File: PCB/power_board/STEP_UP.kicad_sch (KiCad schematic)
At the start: 9 parts, among them IC11 TPS61032PWP, IC8 TPS63000IDRCRQ1

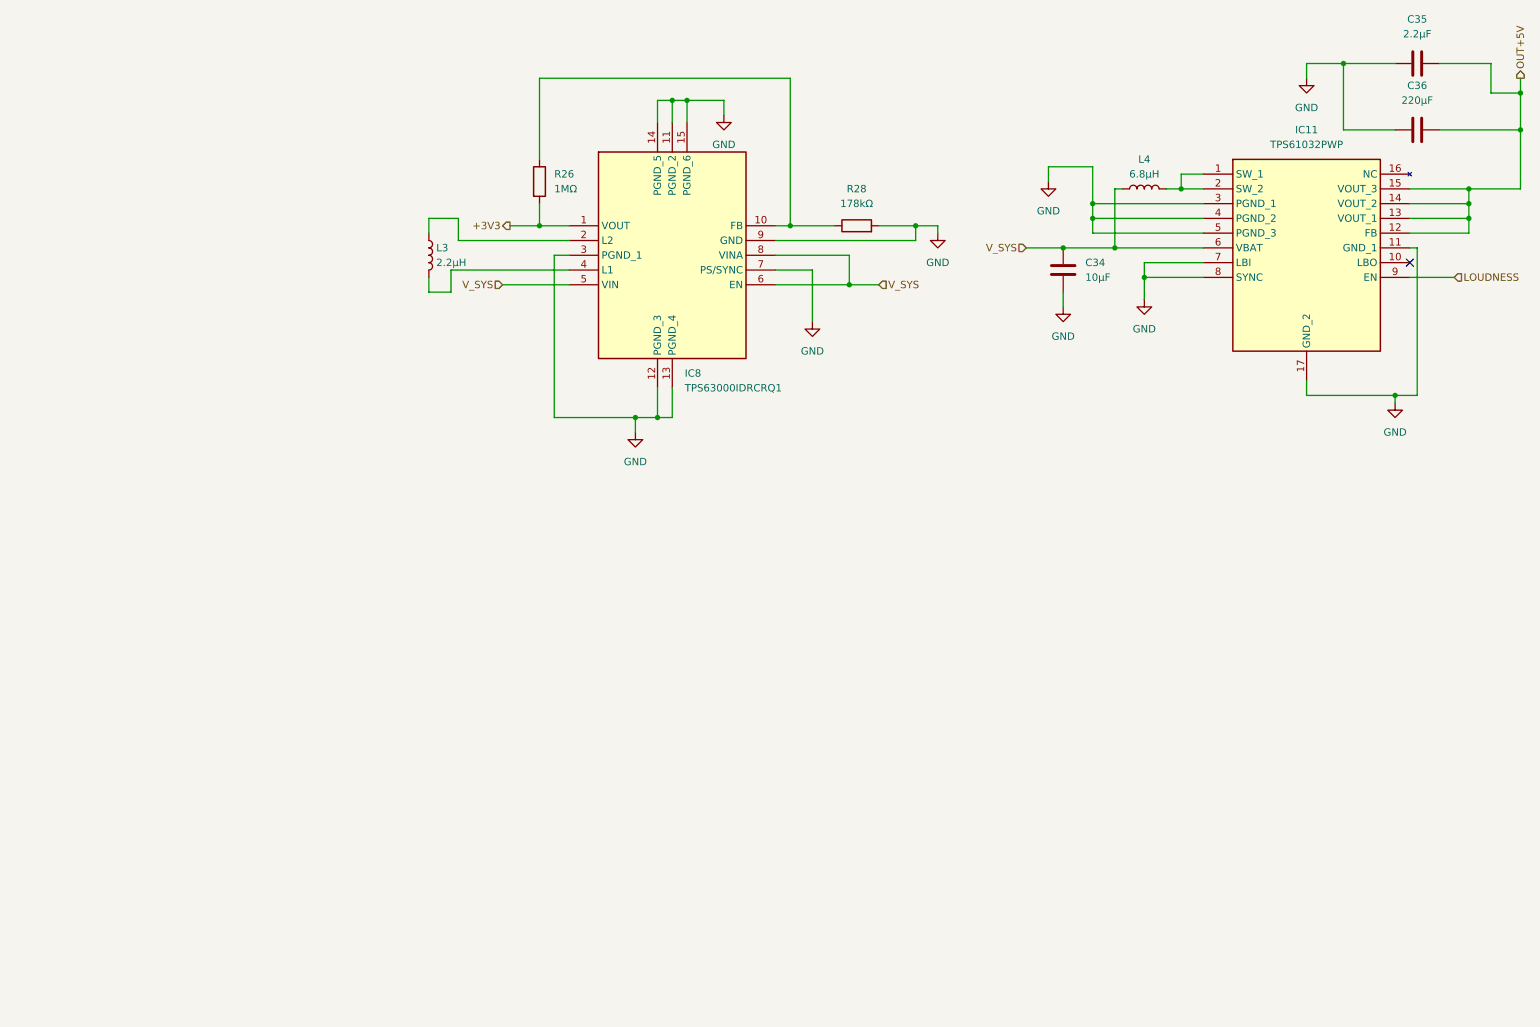
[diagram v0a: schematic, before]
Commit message: verifying schematic and 3V8 power for gsm
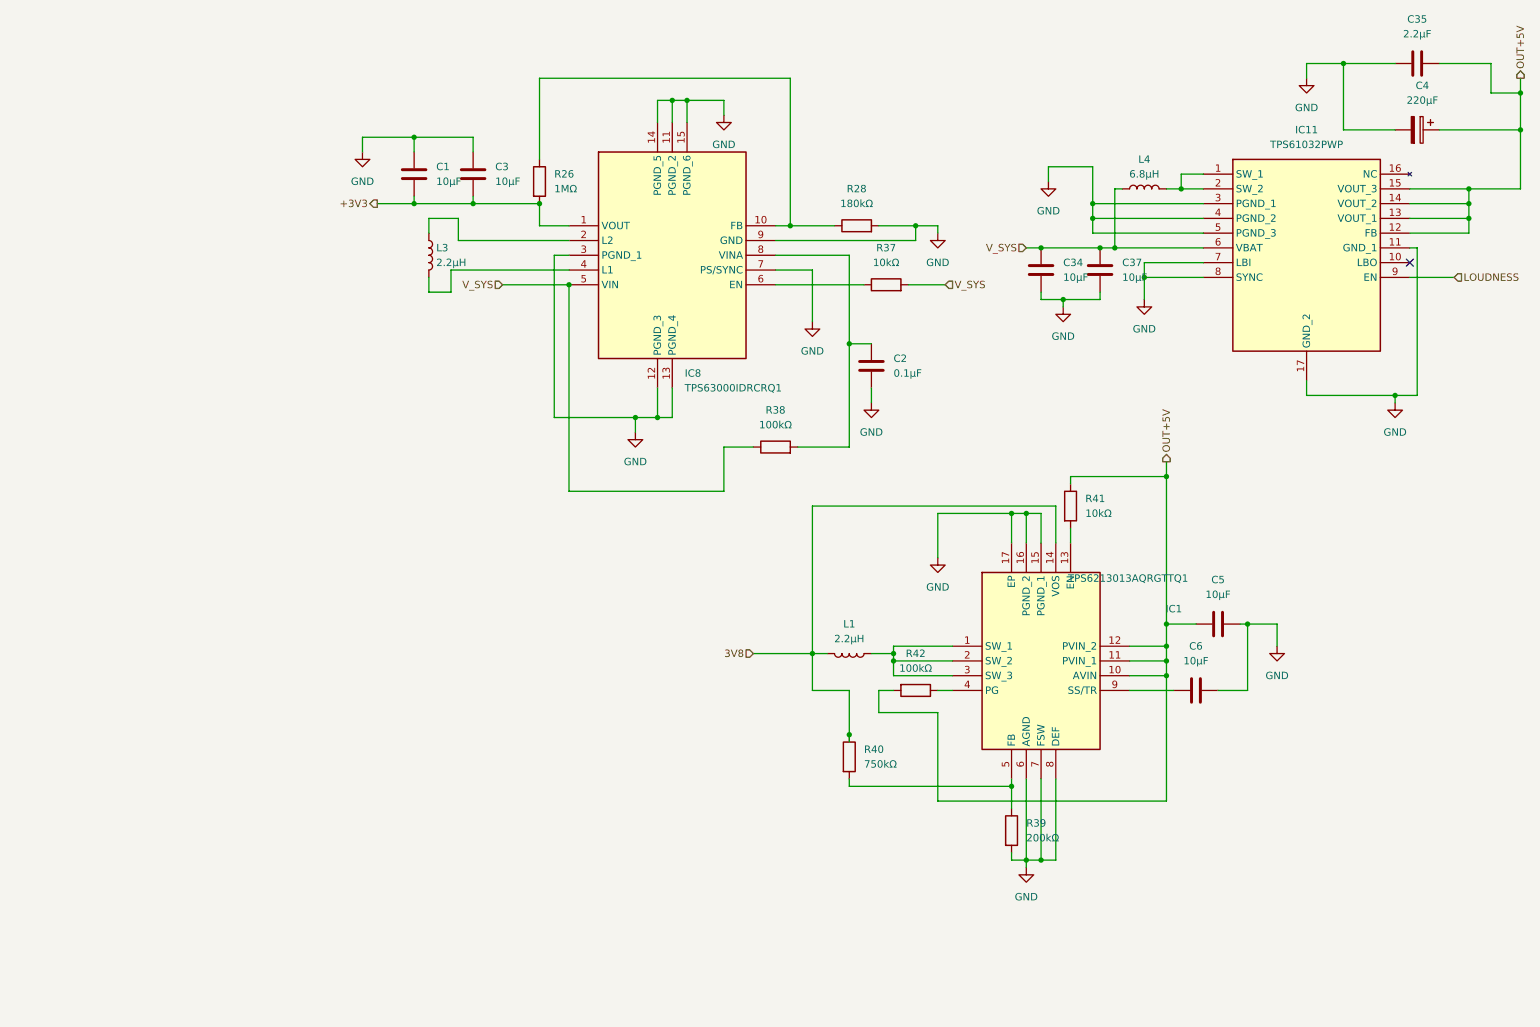
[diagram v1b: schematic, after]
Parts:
- removed C36: 220µF, Capacitor_THT:C_Disc_D5.0mm_W2.5mm_P2.50mm, symbol Device:C
- added C1, C3: 10μF, symbol Device:C
- added C2: 0.1μF, symbol Device:C
- added C37: 10µF, Capacitor_THT:C_Disc_D5.0mm_W2.5mm_P2.50mm, symbol Device:C
- added C4: 220µF, symbol Device:C_Polarized
- added C5, C6: 10µF, symbol Device:C
- added IC1: TPS6213013AQRGTTQ1, QFN50P300X300X100-17N-D, symbol TPS6213013AQRGTTQ1:TPS6213013AQRGTTQ1
- added L1: 2.2µH, symbol Device:L
- added R37, R41: 10kΩ, Resistor_THT:R_Axial_DIN0207_L6.3mm_D2.5mm_P7.62mm_Horizontal, symbol Device:R
- added R38, R42: 100kΩ, Resistor_THT:R_Axial_DIN0207_L6.3mm_D2.5mm_P7.62mm_Horizontal, symbol Device:R
- added R39: 200kΩ, Resistor_THT:R_Axial_DIN0207_L6.3mm_D2.5mm_P7.62mm_Horizontal, symbol Device:R
- added R40: 750kΩ, Resistor_THT:R_Axial_DIN0207_L6.3mm_D2.5mm_P7.62mm_Horizontal, symbol Device:R
- R28: value 178kΩ -> 180kΩ
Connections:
- net +3V3: now also C1.2, C3.2
- net GND: now also C1.1, C2.2, C3.1, C37.2, C4.2, C5.1, C6.1, IC1.15 (PGND_1), IC1.16 (PGND_2), IC1.17 (EP), IC1.6 (AGND), IC1.7 (FSW), IC1.8 (DEF), R39.2
- net OUT+5V: now also C4.1, C5.2, IC1.10 (AVIN), IC1.11 (PVIN_1), IC1.12 (PVIN_2), R41.1, R42.2
- net V_SYS: now also C37.1, R37.2, R38.1; no longer IC8.6 (EN), IC8.8 (VINA)
- new net: IC1.1 (SW_1), IC1.2 (SW_2), IC1.3 (SW_3), L1.1
- new net: IC1.13 (EN), R41.2
- new net: IC1.4 (PG), R42.1
- new net: IC1.5 (FB), R39.1, R40.2
- new net: C6.2, IC1.9 (SS/TR)
- new net: C2.1, IC8.8 (VINA), R38.2
- new net: IC8.6 (EN), R37.1
- new net 3V8: IC1.14 (VOS), L1.2, R40.1
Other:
- moved on the sheet: C34

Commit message: ECR passed
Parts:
- C1, C2, C3, C4, C5, C6: footprint (none) -> Capacitor_THT:C_Disc_D5.0mm_W2.5mm_P2.50mm
- IC1: footprint QFN50P300X300X100-17N-D -> TPS6213013AQRGTTQ1:QFN50P300X300X100-17N-D
- L1: footprint (none) -> Inductor_THT:L_Axial_L7.0mm_D3.3mm_P10.16mm_Horizontal_Fastron_MICC
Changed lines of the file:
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@@
 	)
 	(junction
-		(at 163.83 137.16)
-		(diameter 0)
-		(color 0 0 0 0)
-	)
-	(junction
 		(at 171.45 124.46)
 		(diameter 0)
@@
 	)
 	(junction
+		(at 85.09 45.72)
+		(diameter 0)
+		(color 0 0 0 0)
+	)
+	(junction
 		(at 279.4 26.67)
 		(diameter 0)
@@
 	(wire
 		(pts
-			(xy 163.83 138.43) (xy 163.83 137.16)
-		)
-		(stroke
-			(width 0)
-			(type default)
-		)
-	)
-	(wire
-		(pts
 			(xy 205.74 39.37) (xy 198.12 39.37)
 		)
@@
 	(wire
 		(pts
-			(xy 82.55 45.72) (xy 88.9 45.72)
+			(xy 82.55 45.72) (xy 85.09 45.72)
 		)
 		(stroke
@@
 	(wire
 		(pts
+			(xy 85.09 45.72) (xy 85.09 50.8)
+		)
+		(stroke
+			(width 0)
+			(type default)
+		)
+	)
+	(wire
+		(pts
 			(xy 151.13 49.53) (xy 153.67 49.53)
 		)
@@
 	(wire
 		(pts
+			(xy 85.09 45.72) (xy 88.9 45.72)
+		)
+		(stroke
+			(width 0)
+			(type default)
+		)
+	)
+	(wire
+		(pts
 			(xy 130.81 27.94) (xy 133.35 27.94)
 		)
@@
 	(wire
 		(pts
-			(xy 163.83 137.16) (xy 163.83 129.54)
+			(xy 142.24 95.25) (xy 142.24 87.63)
 		)
 		(stroke
@@
 	(wire
 		(pts
-			(xy 142.24 95.25) (xy 142.24 87.63)
+			(xy 274.32 26.67) (xy 279.4 26.67)
 		)
 		(stroke
@@
 	(wire
 		(pts
-			(xy 274.32 26.67) (xy 279.4 26.67)
+			(xy 163.83 129.54) (xy 163.83 137.16)
 		)
 		(stroke
@@
 			)
 		)
-		(property "Footprint" "QFN50P300X300X100-17N-D"
+		(property "Footprint" "TPS6213013AQRGTTQ1:QFN50P300X300X100-17N-D"
 			(at 208.28 206.68 0)
 			(hide yes)
@@
 			)
 		)
-		(property "Footprint" ""
+		(property "Footprint" "Capacitor_THT:C_Disc_D5.0mm_W2.5mm_P2.50mm"
 			(at 223.52 119.0752 0)
 			(hide yes)
@@
 			)
 		)
-		(property "Footprint" ""
+		(property "Footprint" "Capacitor_THT:C_Disc_D5.0mm_W2.5mm_P2.50mm"
 			(at 89.8652 44.45 0)
 			(hide yes)
@@
 			)
 		)
-		(property "Footprint" ""
+		(property "Footprint" "Inductor_THT:L_Axial_L7.0mm_D3.3mm_P10.16mm_Horizontal_Fastron_MICC"
 			(at 163.83 123.19 0)
 			(hide yes)
@@
 			)
 		)
-		(property "Footprint" ""
+		(property "Footprint" "Capacitor_THT:C_Disc_D5.0mm_W2.5mm_P2.50mm"
 			(at 219.71 130.5052 0)
 			(hide yes)
@@
 			)
 		)
-		(property "Footprint" ""
+		(property "Footprint" "Capacitor_THT:C_Disc_D5.0mm_W2.5mm_P2.50mm"
 			(at 257.81 33.9852 0)
 			(hide yes)
@@
 			)
 		)
-		(property "Footprint" ""
+		(property "Footprint" "Capacitor_THT:C_Disc_D5.0mm_W2.5mm_P2.50mm"
 			(at 100.0252 44.45 0)
 			(hide yes)
@@
 			)
 		)
-		(property "Footprint" ""
+		(property "Footprint" "Capacitor_THT:C_Disc_D5.0mm_W2.5mm_P2.50mm"
 			(at 168.6052 77.47 0)
 			(hide yes)
@@
 					(unit 1)
 				)
+			)
+		)
+	)
+	(symbol
+		(lib_id "power:PWR_FLAG")
+		(at 85.09 50.8 180)
+		(unit 1)
+		(body_style 1)
+		(exclude_from_sim no)
+		(in_bom yes)
+		(on_board yes)
+		(in_pos_files yes)
+		(dnp no)
+		(fields_autoplaced yes)
+		(property "Reference" "#FLG01"
+			(at 85.09 52.705 0)
+			(hide yes)
+			(show_name no)
+			(do_not_autoplace no)
+			(effects
+				(font
+					(size 1.27 1.27)
+				)
+			)
+		)
+		(property "Value" "PWR_FLAG"
+			(at 85.09 55.88 0)
+			(show_name no)
+			(do_not_autoplace no)
+			(effects
+				(font
+					(size 1.27 1.27)
+				)
+			)
+		)
+		(property "Footprint" ""
+			(at 85.09 50.8 0)
+			(hide yes)
+			(show_name no)
+			(do_not_autoplace no)
+			(effects
+				(font
+					(size 1.27 1.27)
+				)
+			)
+		)
+		(property "Datasheet" ""
+			(at 85.09 50.8 0)
+			(hide yes)
+			(show_name no)
+			(do_not_autoplace no)
+			(effects
+				(font
+					(size 1.27 1.27)
+				)
+			)
+		)
+		(property "Description" "Special symbol for telling ERC where power comes from"
+			(at 85.09 50.8 0)
+			(hide yes)
+			(show_name no)
+			(do_not_autoplace no)
+			(effects
+				(font
+					(size 1.27 1.27)
+				)
+			)
+		)
+		(pin "1"
+		)
+		(instances
+			(project "power_board"
+				(path "/f044e945-eb74-49fa-825d-5f99d2d7b949/ffe405b2-78da-4851-81d5-f45dbb795d0e"
+					(reference "#FLG01")
+					(unit 1)
+				)

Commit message: imu from board
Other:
- moved on the sheet: C1, C2, C3, C5, C6, IC1, IC8, L1, L3, R26, R28, R37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

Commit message: before smd
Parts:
- removed C1, C3: 10μF, Capacitor_THT:C_Disc_D5.0mm_W2.5mm_P2.50mm, symbol Device:C
- removed C2: 0.1μF, Capacitor_THT:C_Disc_D5.0mm_W2.5mm_P2.50mm, symbol Device:C
- removed IC1: TPS6213013AQRGTTQ1, TPS6213013AQRGTTQ1:QFN50P300X300X100-17N-D, symbol TPS6213013AQRGTTQ1:TPS6213013AQRGTTQ1
- removed IC8: TPS63000IDRCRQ1, TPS63000IDRCRQ1:TPS63000IDRCRQ1, symbol TPS63000IDRCRQ1:TPS63000IDRCRQ1
- removed L1, L3: 2.2µH, Inductor_THT:L_Axial_L7.0mm_D3.3mm_P10.16mm_Horizontal_Fastron_MICC, symbol Device:L
- removed R26: 1MΩ, Resistor_THT:R_Axial_DIN0207_L6.3mm_D2.5mm_P7.62mm_Horizontal, symbol Device:R
- removed R28: 180kΩ, Resistor_THT:R_Axial_DIN0207_L6.3mm_D2.5mm_P7.62mm_Horizontal, symbol Device:R
- removed R37, R41: 10kΩ, Resistor_THT:R_Axial_DIN0207_L6.3mm_D2.5mm_P7.62mm_Horizontal, symbol Device:R
- removed R38, R42: 100kΩ, Resistor_THT:R_Axial_DIN0207_L6.3mm_D2.5mm_P7.62mm_Horizontal, symbol Device:R
- removed R39: 200kΩ, Resistor_THT:R_Axial_DIN0207_L6.3mm_D2.5mm_P7.62mm_Horizontal, symbol Device:R
- removed R40: 750kΩ, Resistor_THT:R_Axial_DIN0207_L6.3mm_D2.5mm_P7.62mm_Horizontal, symbol Device:R
- added C1: 100μF, Capacitor_Tantalum_SMD:CP_EIA-3216-18_Kemet-A, symbol Device:C_Polarized
- added D2: LED, LED_SMD:LED_0603_1608Metric, symbol Device:LED
- added IC1: TPS61131PW, TPS61131PW:SOP65P640X120-16N, symbol TPS61131PW:TPS61131PW
- added L5: 22µH, Inductor_SMD:L_6.3x6.3_H3, symbol Device:L
- added L6: 22µH, Inductor_THT:L_Axial_L7.0mm_D3.3mm_P10.16mm_Horizontal_Fastron_MICC, symbol Device:L
- added R1: 1MΩ, Resistor_SMD:R_0603_1608Metric, symbol Device:R
- added R2: 200kΩ, Resistor_SMD:R_0603_1608Metric, symbol Device:R
- added R3, R5: 100kΩ, Resistor_SMD:R_0603_1608Metric, symbol Device:R
- added R6: 1kΩ, Resistor_SMD:R_0603_1608Metric, symbol Device:R
- C34, C35, C37, C4: footprint Capacitor_THT:C_Disc_D5.0mm_W2.5mm_P2.50mm -> Capacitor_SMD:CP_Elec_6.3x5.4
- C5: value 10µF -> 10μF; footprint Capacitor_THT:C_Disc_D5.0mm_W2.5mm_P2.50mm -> Capacitor_SMD:CP_Elec_6.3x5.4
- C6: value 10µF -> 10u X7R; footprint Capacitor_THT:C_Disc_D5.0mm_W2.5mm_P2.50mm -> Capacitor_SMD:CP_Elec_6.3x5.4
- L4: footprint Inductor_THT:L_Axial_L7.0mm_D3.3mm_P10.16mm_Horizontal_Fastron_MICC -> Inductor_SMD:L_6.3x6.3_H3
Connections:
- net +3V3: now also C1.1, D2.2 (A), IC1.16 (VOUT), R5.1
- net GND: now also C5.2, C1.2, IC1.10 (LDOOUT), IC1.11 (LDOSENSE), IC1.12 (GND), IC1.15 (FB), IC1.3 (PGND), IC1.6 (SKIPEN), IC1.9 (LDOIN), L6.2, R2.2; no longer C5.1, C6.1
- net OUT+5V: no longer C5.2
- net V_SYS: now also C5.1, IC1.4 (VBAT), IC1.7 (EN), IC1.8 (LDOEN), L5.2, R1.1
- net at C6.2: now also IC1.2 (SWN), L5.1
- new net: R1.2, R3.1
- new net: C6.1, IC1.1 (SWP), L6.1
- new net: IC1.13 (LBO), R6.2
- new net: IC1.14 (PGOOD), R5.2
- new net: IC1.5 (LBI), R2.1, R3.2
- new net: D2.1 (K), R6.1

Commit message: goldpins on one side
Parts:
- L6: footprint Inductor_THT:L_Axial_L7.0mm_D3.3mm_P10.16mm_Horizontal_Fastron_MICC -> Inductor_SMD:L_6.3x6.3_H3
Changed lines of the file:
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@@
 			)
 		)
-		(property "Footprint" "Inductor_THT:L_Axial_L7.0mm_D3.3mm_P10.16mm_Horizontal_Fastron_MICC"
+		(property "Footprint" "Inductor_SMD:L_6.3x6.3_H3"
 			(at 77.47 73.66 0)
 			(hide yes)

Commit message: modified gnd
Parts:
- L6: footprint Inductor_SMD:L_6.3x6.3_H3 -> Inductor_THT:L_Axial_L7.0mm_D3.3mm_P10.16mm_Horizontal_Fastron_MICC
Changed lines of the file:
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@@
 			)
 		)
-		(property "Footprint" "Inductor_SMD:L_6.3x6.3_H3"
+		(property "Footprint" "Inductor_THT:L_Axial_L7.0mm_D3.3mm_P10.16mm_Horizontal_Fastron_MICC"
 			(at 77.47 73.66 0)
 			(hide yes)
